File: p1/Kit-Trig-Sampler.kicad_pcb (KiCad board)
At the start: 2 copper layers, 78 x 109.2 mm, 79 parts, among them J1 START_CV, J10 AUDIO_INR, J11 AUDIO_OUTL, J12 Eurorack_Power_16pin_Unshroud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, J2 LENGTH_CV, J3 SAMP_CV, J4 PITCH CV, J5 REV_TRIG, J6 PLAY_TRIG, J7 END_OUT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

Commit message: Small changes to pin assignments
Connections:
- C1 pad 1: /A4 -> /A1
- C10 pad 1: /A6 -> /A3
- C18 pad 1: /A9 -> /A6
- C2 pad 1: /A5 -> /A9
- J5 pad 1: /D15 -> /D2
- POT_PITCH1 pad 2: /A4 -> /A1
- POT_SAMP1 pad 2: /A5 -> /A9
- POT_START1 pad 2: /A6 -> /A3
- R12 pad 1: /D2 -> /D15
- R18 pad 1: /D7 -> /D11
- R19 pad 1: /D3 -> /D12
- R20 pad 1: /D10 -> /D5
- R21 pad 1: /D12 -> /D7
- R24 pad 2: /D11 -> /D3
- R27 pad 2: /A9 -> /A6
- R28 pad 2: /D18 -> /D19
- R3 pad 2: /A1 -> /A5
- R30 pad 2: /D19 -> /D18
- R31 pad 2: /D16 -> /D17
- R32 pad 2: /D17 -> /D16
- R4 pad 2: /A3 -> /A8
- R6 pad 2: /A1 -> /A5
- R7 pad 2: /A3 -> /A8
- SD1 pad 1: /D18 -> /D19
- SD1 pad 3: /D19 -> /D18
- SD1 pad 7: /D16 -> /D17
- SD1 pad 8: /D17 -> /D16

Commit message: added Bank cv
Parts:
- added J12: Eurorack_Power_16pin_Unshrouded, 4ms_Jack:EighthInch_PJ398SM, B.Cu at (-12.4, 85.8)
- added R33: 47k_TH0.125, 4ms_Resistor:R_Axial_DIN0207_L6.3mm_D2.5mm_P7.62mm_Horizontal, F.Cu at (79.2, 84.8)
- added R34: 100k_TH0.125, 4ms_Resistor:R_Axial_DIN0207_L6.3mm_D2.5mm_P7.62mm_Horizontal, F.Cu at (93.6, 73.3)
- J13: renamed from J12; value Eurorack_Power_16pin_Unshrouded -> BANK_CV
- moved J6 18.3 mm to (-30.7, 85.8)
- moved J5 15.4 mm to (-30.7, 101.2)
- moved J7 9.16 mm to (-12.4, 101.2)
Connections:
- J13 pad 1: /PWR_HDR_CLK_BUS -> Net-(J13-Pad1)
- J13 pad 10: GND -> (no net)
- J13 pad 11: GND -> (no net)
- J13 pad 12: GND -> (no net)
- J13 pad 13: GND -> (no net)
- J13 pad 14: GND -> (no net)
- J13 pad 15: Net-(D2-Pad1) -> (no net)
- J13 pad 16: Net-(D2-Pad1) -> (no net)
- J13 pad 2: /PWR_HDR_CLK_BUS -> GND
- J13 pad 3: unconnected-(J12-Pad3) -> GND
- J13 pad 4: unconnected-(J12-Pad4) -> (no net)
- J13 pad 5: unconnected-(J12-Pad5) -> (no net)
- J13 pad 6: unconnected-(J12-Pad6) -> (no net)
- J13 pad 7: Net-(D1-Pad2) -> (no net)
- J13 pad 8: Net-(D1-Pad2) -> (no net)
- J13 pad 9: GND -> (no net)
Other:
- board text added: "BANK_CV"

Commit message: part placement ip
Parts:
- J13: renamed from J12; value Eurorack_Power_16pin_Unshrouded -> BANK_CV
- J14: renamed from J13; value BANK_CV -> Eurorack_Power_16pin_Unshrouded
- moved C1 270.3 mm to (156.3, -12.2)
- moved C10 270.3 mm to (111.6, 33.1)
- moved C17 270.3 mm to (157.0, -16.3)
- moved C18 270.3 mm to (122.8, 19.5)
- moved C2 270.3 mm to (132.1, 6.16)
- moved C9 270.3 mm to (140.1, 5.91)
- moved R17 270.3 mm to (105.4, 18.0)
- moved R2 270.3 mm to (83.6, 33.4)
- moved R22 270.3 mm to (137.0, -16.6)
- moved R25 270.3 mm to (83.6, 40.5)
- moved R27 270.3 mm to (69.2, 44.8)
- moved R28 270.3 mm to (79.8, 44.8)
- moved R29 270.3 mm to (94.8, 21.6)
- moved R3 270.3 mm to (112.2, 10.0)
- moved R30 270.3 mm to (105.4, 21.6)
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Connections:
- J13 pad 1: /PWR_HDR_CLK_BUS -> Net-(J13-Pad1)
- J13 pad 2: /PWR_HDR_CLK_BUS -> GND
- J13 pad 3: unconnected-(J12-Pad3) -> GND
- J14 pad 1: Net-(J13-Pad1) -> /PWR_HDR_CLK_BUS
- J14 pad 10: (no net) -> GND
- J14 pad 11: (no net) -> GND
- J14 pad 12: (no net) -> GND
- J14 pad 13: (no net) -> GND
- J14 pad 14: (no net) -> GND
- J14 pad 15: (no net) -> Net-(D2-Pad1)
- J14 pad 16: (no net) -> Net-(D2-Pad1)
- J14 pad 2: GND -> /PWR_HDR_CLK_BUS
- J14 pad 3: GND -> unconnected-(J14-Pad3)
- J14 pad 4: (no net) -> unconnected-(J14-Pad4)
- J14 pad 5: (no net) -> unconnected-(J14-Pad5)
- J14 pad 6: (no net) -> unconnected-(J14-Pad6)
- J14 pad 7: (no net) -> Net-(D1-Pad2)
- J14 pad 8: (no net) -> Net-(D1-Pad2)
- J14 pad 9: (no net) -> GND
- R24 pad 2: /D3 -> /D10
- U2 pad 1: (no net) -> Net-(C11-Pad2)
- U2 pad 2: (no net) -> Net-(C11-Pad1)
- U2 pad 3: (no net) -> Net-(R12-Pad2)
- U2 pad 5: Net-(R12-Pad2) -> (no net)
- U2 pad 6: Net-(C11-Pad1) -> (no net)
- U2 pad 7: Net-(C11-Pad2) -> (no net)

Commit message: part placement pending approval
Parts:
- moved C9 168.5 mm to (-17.1, 66.4), turned to 180 degrees
- moved C17 162.8 mm to (-2.65, 15.4)
- moved C18 158.5 mm to (-35.7, 17.8), turned to -90 degrees
- moved R6 154.0 mm to (-0.40, 56.4), turned to -90 degrees
- moved C2 153.1 mm to (-17.7, 37.8)
- moved C1 145.6 mm to (19.4, 37.4), turned to 90 degrees
- moved R7 130.3 mm to (-28.0, 77.5)
- moved R4 126.5 mm to (-18.7, 73.8), turned to -90 degrees
- moved R3 125.8 mm to (-3.80, 58.7), turned to -90 degrees
- moved R32 125.5 mm to (-10.3, 34.0)
- moved R27 105.4 mm to (-31.9, 15.0), turned to -90 degrees
- moved R22 105.4 mm to (34.5, 7.70), turned to -90 degrees
- moved C10 99.6 mm to (18.0, 67.4)
- moved R28 99.4 mm to (-17.4, 24.0), turned to 90 degrees
- moved R31 97.5 mm to (8.70, 37.6), turned to 180 degrees
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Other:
- board text added: "STS KIT p1"

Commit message: small updates
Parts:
- Bank_But1: renamed from BANK_BUT1; footprint 4ms_Switch:Button_RgbLED_SPST_PB615303HL-7mm -> 4ms_Switch:Button_RgbLED_SPST_TC002
- REV_BUT1: footprint 4ms_Switch:Button_RgbLED_SPST_PB615303HL-7mm -> 4ms_Switch:Button_RgbLED_SPST_TC002
- moved C12 1.90 mm to (21.8, 46.9)
- moved R19 1.65 mm to (8.50, 25.0)
- moved R8 0.90 mm to (24.8, 63.1)
- moved R11 0.76 mm to (32.8, 56.1)
- moved R31 0.71 mm to (8.60, 38.3)
- moved R10 0.70 mm to (30.7, 48.6)
- moved R9 0.60 mm to (36.8, 56.4)
- moved R30 0.20 mm to (8.70, 33.8)

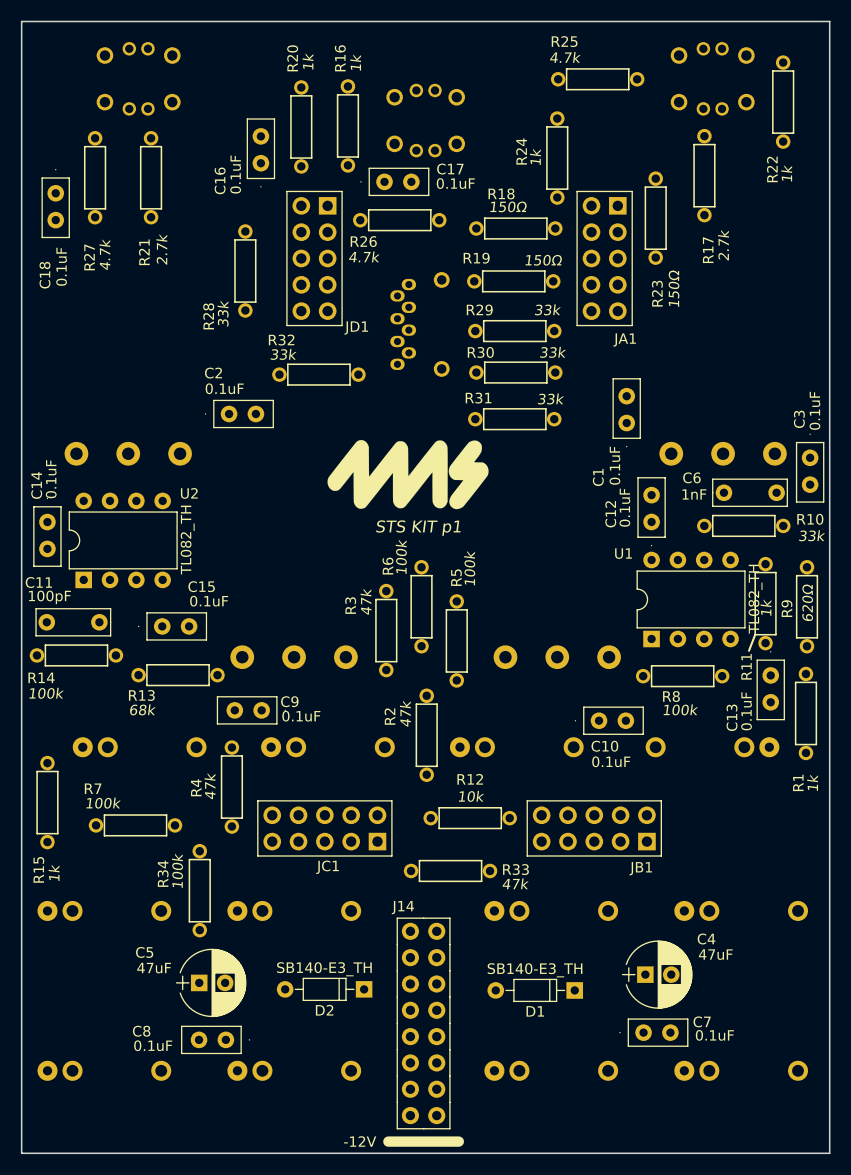
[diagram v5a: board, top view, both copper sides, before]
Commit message: Finished routing
needs a once over and silk arrangement.
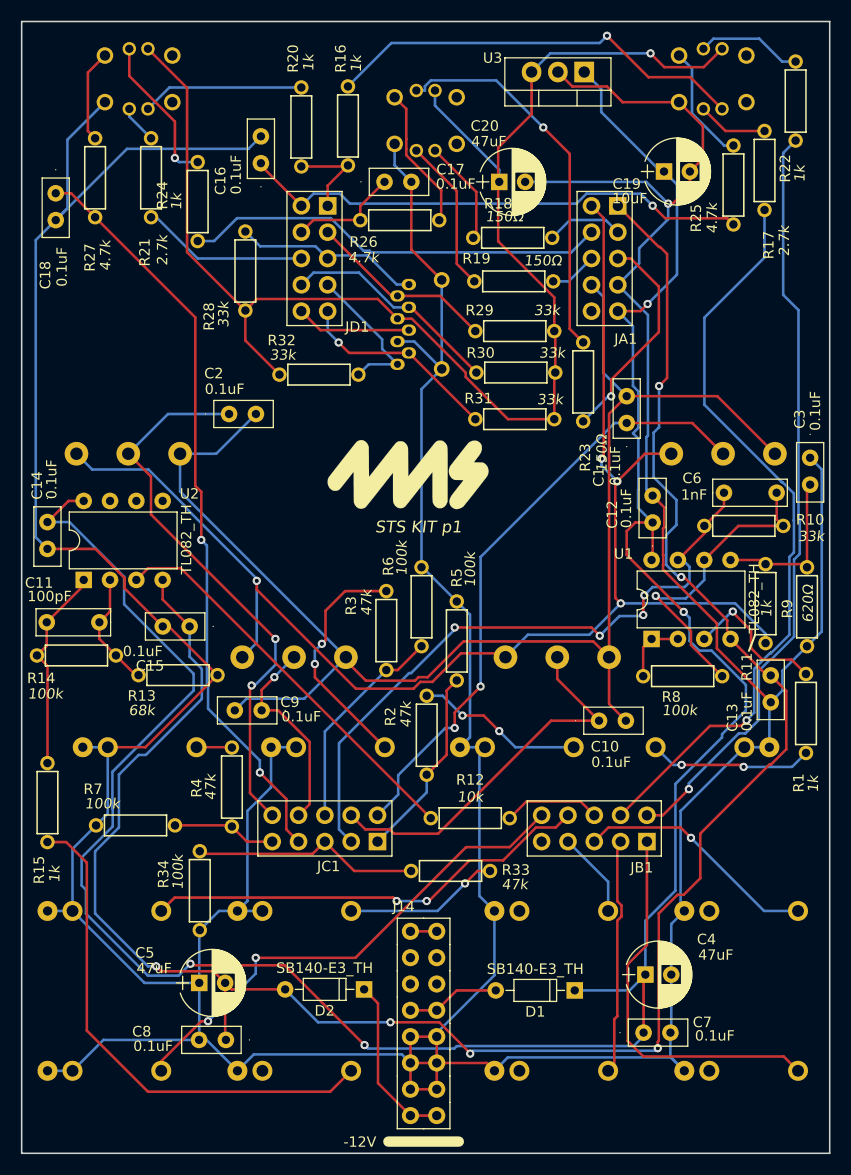
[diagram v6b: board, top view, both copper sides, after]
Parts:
- added C19: 10uF_Radial_TH, 4ms_Capacitor:CP_Radial_P2.5mm, F.Cu at (23.0, 14.4)
- added C20: 47uF_16V_TH, 4ms_Capacitor:CP_Radial_P2.5mm, F.Cu at (7.10, 15.4)
- added U3: 78M33_TH, Package_TO_SOT_THT:TO-220-3_Vertical, F.Cu at (15.3, 4.80)
- moved R24 35.0 mm to (-22.0, 17.3)
- moved R23 17.3 mm to (15.2, 34.7)
- moved R25 16.6 mm to (29.7, 15.7), turned to -90 degrees
- moved R17 5.82 mm to (32.7, 14.3)
- moved R22 1.20 mm to (35.7, 7.60)
- moved R18 0.95 mm to (8.40, 20.8)
- moved C12 0.11 mm to (21.9, 47.0)
- turned C15 to 180 degrees
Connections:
- JD1 pad 8: +3V3 -> /D4
- R28 pad 2: /D19 -> /D18
- R29 pad 2: Net-(R29-Pad2) -> /D19
- R30 pad 2: /D18 -> /D4
- R31 pad 2: /D17 -> /D16
- R32 pad 2: /D16 -> /D17
- SD1 pad 1: /D19 -> /D18
- SD1 pad 2: Net-(R29-Pad2) -> /D19
- SD1 pad 3: /D18 -> /D4
- SD1 pad 7: /D17 -> /D16
- SD1 pad 8: /D16 -> /D17
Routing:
- net GND: track 0.00 -> 524.5 mm, vias 0 -> 1
- net +12V: track 0.00 -> 238.8 mm, vias 0 -> 4
- net -12VA: track 0.00 -> 198.8 mm, vias 0 -> 6
- net +3V3: track 0.00 -> 140.7 mm, vias 0 -> 1
- net GNDADC: track 0.00 -> 137.9 mm
- net VREF+: track 0.00 -> 136.0 mm, vias 0 -> 4
- net /D0: track 0.00 -> 73.7 mm, vias 0 -> 1
- net /D1: track 0.00 -> 73.2 mm, vias 0 -> 1
- net /A6: track 0.00 -> 73.1 mm, vias 0 -> 2
- net /A2: track 0.00 -> 62.9 mm, vias 0 -> 4
- net /A1: track 0.00 -> 59.6 mm, vias 0 -> 2
- net /A9: track 0.00 -> 54.2 mm, vias 0 -> 2
- net /D6: track 0.00 -> 49.7 mm, vias 0 -> 1
- net Net-(J7-Pad1): track 0.00 -> 49.6 mm
- net /D2: track 0.00 -> 48.4 mm, vias 0 -> 2
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
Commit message: finished routing and silk arrangement
ready for review
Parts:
- moved R31 3.57 mm to (8.86, 41.9)
- moved R30 2.93 mm to (8.76, 36.7)
- moved G***1 2.41 mm to (-4.09, 43.9)
- moved R29 1.63 mm to (8.76, 31.4)
- moved R19 1.22 mm to (8.33, 26.2)
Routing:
- net +3V3: track 140.7 -> 147.5 mm, vias 1 -> 2
- net /D16: track 19.7 -> 23.4 mm
- net /D4: track 21.2 -> 24.1 mm
- net /D19: track 18.2 -> 19.9 mm
- net Net-(PLAY_BUT1-Pad7): track 14.9 -> 16.1 mm
- net /D12: track 4.61 -> 5.28 mm
